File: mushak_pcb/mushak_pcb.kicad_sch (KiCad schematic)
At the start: 48 parts, among them J1 Conn_01x04_Male, J10 IR_1, J11 AS5600_1, J12 IR_2, J13 AS5600_2, J14 IR_3, J15 ToF, J16 IR_4, J2 Conn_01x02_Female, J3 BLE_Conn, Q1 DMN3065LW-7, SW1 SW_Push, SW2 SW_Push, U1 BA30BC0FP-E2, U6 STM32F405RGTx, Y1 25Mhz, Y2 32.769kHz

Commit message: completed routing
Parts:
- J2: footprint Connector_JST:JST_SHL_SM02B-SHLS-TF_1x02-1MP_P1.00mm_Horizontal -> Connector_JST:JST_EH_B2B-EH-A_1x02_P2.50mm_Vertical
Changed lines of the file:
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@@
     (property "Reference" "J2" (id 0) (at 186.055 20.32 0))
     (property "Value" "Conn_01x02_Female" (id 1) (at 186.055 22.86 0))
-    (property "Footprint" "Connector_JST:JST_SHL_SM02B-SHLS-TF_1x02-1MP_P1.00mm_Horizontal" (id 2) (at 185.42 28.448 0)
+    (property "Footprint" "Connector_JST:JST_EH_B2B-EH-A_1x02_P2.50mm_Vertical" (id 2) (at 185.42 28.448 0)
       (effects (font (size 1.27 1.27)) hide)
     )
@@
     )
     (path "/694b3d6e-79ba-4555-820c-469fe372e4c1"
-      (reference "J2") (unit 1) (value "Conn_01x02_Female") (footprint "Connector_JST:JST_SHL_SM02B-SHLS-TF_1x02-1MP_P1.00mm_Horizontal")
+      (reference "J2") (unit 1) (value "Conn_01x02_Female") (footprint "Connector_JST:JST_EH_B2B-EH-A_1x02_P2.50mm_Vertical")
     )
     (path "/be764d54-1c1d-4212-b9f1-489fc6581cc4"

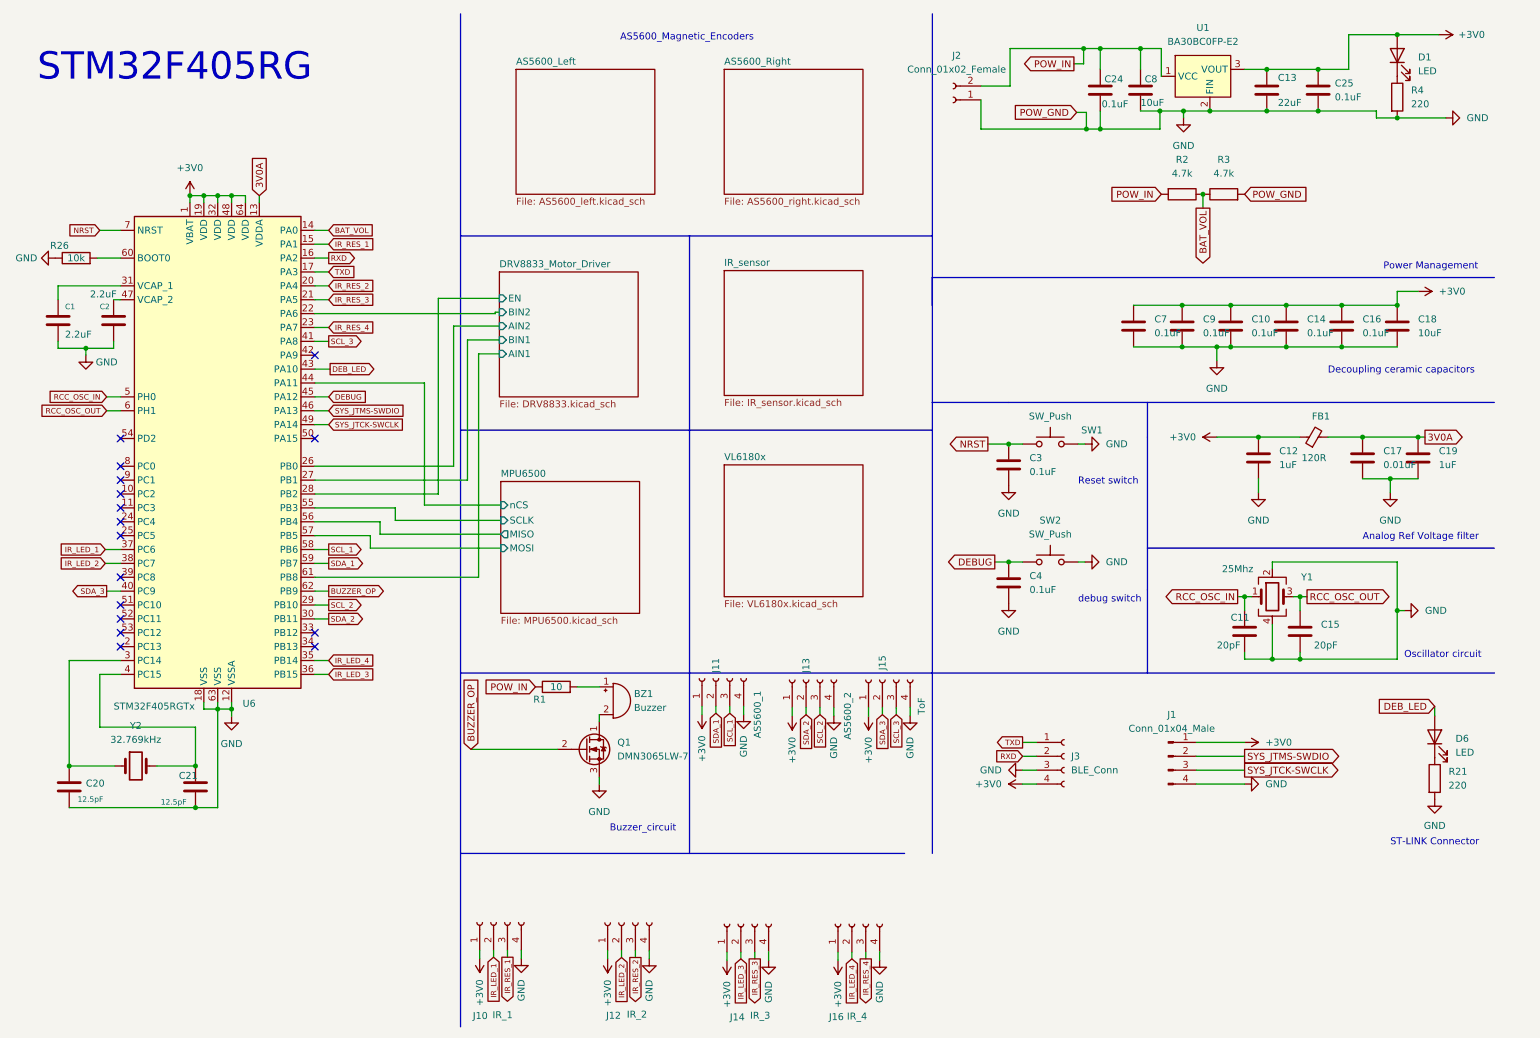
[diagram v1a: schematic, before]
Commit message: changed oscilattor placement
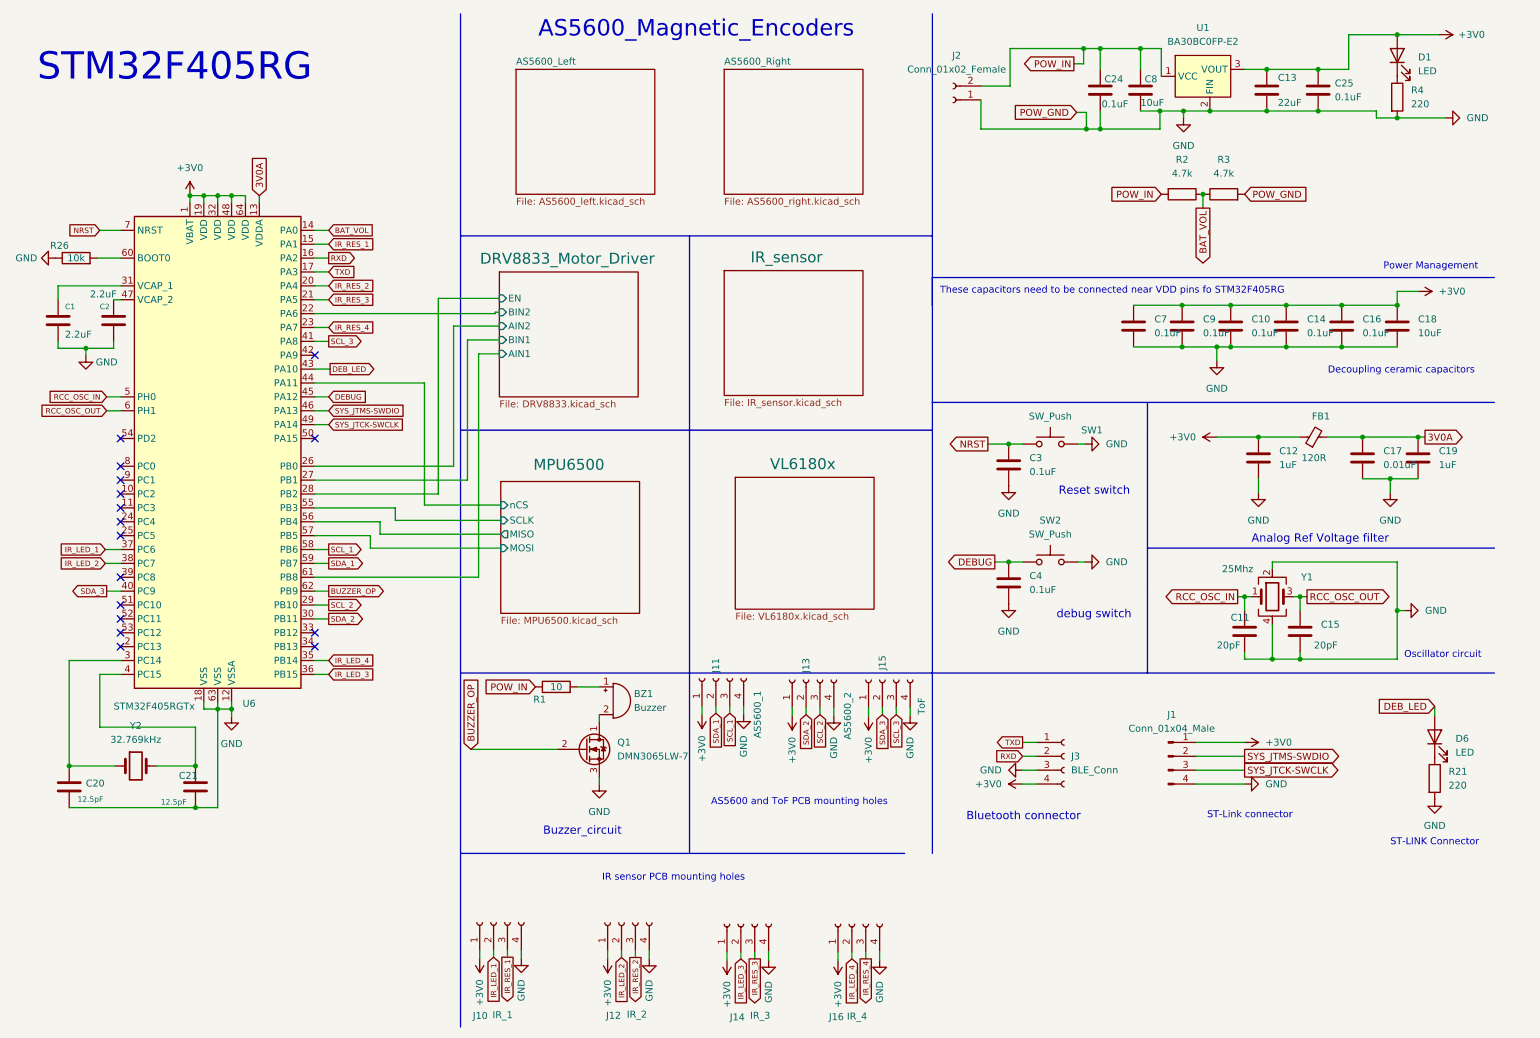
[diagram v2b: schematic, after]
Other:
- note added: "AS5600 and ToF PCB mounting holes"
- note added: "Bluetooth connector"
- note added: "IR sensor PCB mounting holes"
- note added: "ST-Link connector"
- note added: "These capacitors need to be connected near VDD pins fo STM32F405RG"
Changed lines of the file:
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@@
     (effects (font (size 1.27 1.27)) (justify left bottom))
   )
-  (text "debug switch" (at 208.28 120.65 0)
-    (effects (font (size 1.27 1.27)) (justify left bottom))
+  (text "debug switch" (at 204.343 123.571 0)
+    (effects (font (size 1.5 1.5)) (justify left bottom))
   )
   (text "Decoupling ceramic capacitors\n" (at 254 78.74 0)
     (effects (font (size 1.27 1.27)) (justify left bottom))
   )
+  (text "Bluetooth connector\n" (at 187.833 160.528 0)
+    (effects (font (size 1.5 1.5)) (justify left bottom))
+  )
+  (text "ST-Link connector" (at 231.902 160.147 0)
+    (effects (font (size 1.27 1.27)) (justify left bottom))
+  )
   (text "ST-LINK Connector\n" (at 265.43 165.1 0)
     (effects (font (size 1.27 1.27)) (justify left bottom))
   )
-  (text "Analog Ref Voltage filter\n" (at 260.35 109.22 0)
+  (text "Analog Ref Voltage filter\n" (at 240.03 109.728 0)
+    (effects (font (size 1.5 1.5)) (justify left bottom))
+  )
+  (text "Buzzer_circuit" (at 110.363 163.195 0)
+    (effects (font (size 1.5 1.5)) (justify left bottom))
+  )
+  (text "AS5600 and ToF PCB mounting holes" (at 141.097 157.734 0)
     (effects (font (size 1.27 1.27)) (justify left bottom))
   )
-  (text "Buzzer_circuit" (at 122.555 162.56 0)
+  (text "IR sensor PCB mounting holes" (at 121.158 171.577 0)
     (effects (font (size 1.27 1.27)) (justify left bottom))
   )
-  (text "Reset switch\n" (at 208.28 99.06 0)
-    (effects (font (size 1.27 1.27)) (justify left bottom))
-  )
-  (text "AS5600_Magnetic_Encoders\n" (at 124.46 17.78 0)
-    (effects (font (size 1.27 1.27)) (justify left bottom))
+  (text "Reset switch\n" (at 204.724 100.965 0)
+    (effects (font (size 1.5 1.5)) (justify left bottom))
+  )
+  (text "AS5600_Magnetic_Encoders\n" (at 109.474 17.272 0)
+    (effects (font (size 3 3)) (justify left bottom))
   )
   (text "STM32F405RG\n" (at 17.78 25.4 0)
     (effects (font (size 5 5)) (justify left bottom))
+  )
+  (text "These capacitors need to be connected near VDD pins fo STM32F405RG"
+    (at 183.007 64.135 0)
+    (effects (font (size 1.27 1.27)) (justify left bottom))
   )
   (text "Oscillator circuit\n" (at 267.97 130.81 0)
@@
     )
   )
-  (sheet (at 143.51 95.25) (size 25.4 24.13) (fields_autoplaced)
+  (sheet (at 145.542 97.536) (size 25.4 24.13)
     (stroke (width 0.1524) (type solid) (color 0 0 0 0))
     (fill (color 0 0 0 0.0000))
-    (property "Sheet name" "VL6180x" (id 0) (at 143.51 94.5384 0)
-      (effects (font (size 1.27 1.27)) (justify left bottom))
-    )
-    (property "Sheet file" "VL6180x.kicad_sch" (id 1) (at 143.51 119.9646 0)
+    (property "Sheet name" "VL6180x" (id 0) (at 151.892 96.266 0)
+      (effects (font (size 2 2)) (justify left bottom))
+    )
+    (property "Sheet file" "VL6180x.kicad_sch" (id 1) (at 145.542 122.2506 0)
       (effects (font (size 1.27 1.27)) (justify left top))
     )
@@
     )
   )
-  (sheet (at 102.616 98.298) (size 25.4 24.13) (fields_autoplaced)
+  (sheet (at 102.616 98.298) (size 25.4 24.13)
     (stroke (width 0.1524) (type solid) (color 0 0 0 0))
     (fill (color 0 0 0 0.0000))
-    (property "Sheet name" "MPU6500" (id 0) (at 102.616 97.5864 0)
-      (effects (font (size 1.27 1.27)) (justify left bottom))
+    (property "Sheet name" "MPU6500" (id 0) (at 108.585 96.393 0)
+      (effects (font (size 2 2)) (justify left bottom))
     )
     (property "Sheet file" "MPU6500.kicad_sch" (id 1) (at 102.616 123.0126 0)
@@
     )
   )
-  (sheet (at 143.51 59.69) (size 25.4 22.86) (fields_autoplaced)
+  (sheet (at 143.51 59.69) (size 25.4 22.86)
     (stroke (width 0.1524) (type solid) (color 0 0 0 0))
     (fill (color 0 0 0 0.0000))
-    (property "Sheet name" "IR_sensor" (id 0) (at 143.51 58.9784 0)
-      (effects (font (size 1.27 1.27)) (justify left bottom))
+    (property "Sheet name" "IR_sensor" (id 0) (at 148.336 58.42 0)
+      (effects (font (size 2 2)) (justify left bottom))
     )
     (property "Sheet file" "IR_sensor.kicad_sch" (id 1) (at 143.51 83.1346 0)
@@
     )
   )
-  (sheet (at 102.362 59.944) (size 25.4 22.86) (fields_autoplaced)
+  (sheet (at 102.362 59.944) (size 25.4 22.86)
     (stroke (width 0.1524) (type solid) (color 0 0 0 0))
     (fill (color 0 0 0 0.0000))
-    (property "Sheet name" "DRV8833_Motor_Driver" (id 0) (at 102.362 59.2324 0)
-      (effects (font (size 1.27 1.27)) (justify left bottom))
+    (property "Sheet name" "DRV8833_Motor_Driver" (id 0) (at 98.806 58.674 0)
+      (effects (font (size 2 2)) (justify left bottom))
     )
     (property "Sheet file" "DRV8833.kicad_sch" (id 1) (at 102.362 83.3886 0)
